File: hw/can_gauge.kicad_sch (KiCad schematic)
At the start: 22 parts, among them U1 MCP2515-xSO, U2 ULN2003A, U3 ULN2003A, U4 ULN2003A, U5 74HC595, U6 74HC595, U7 74HC595

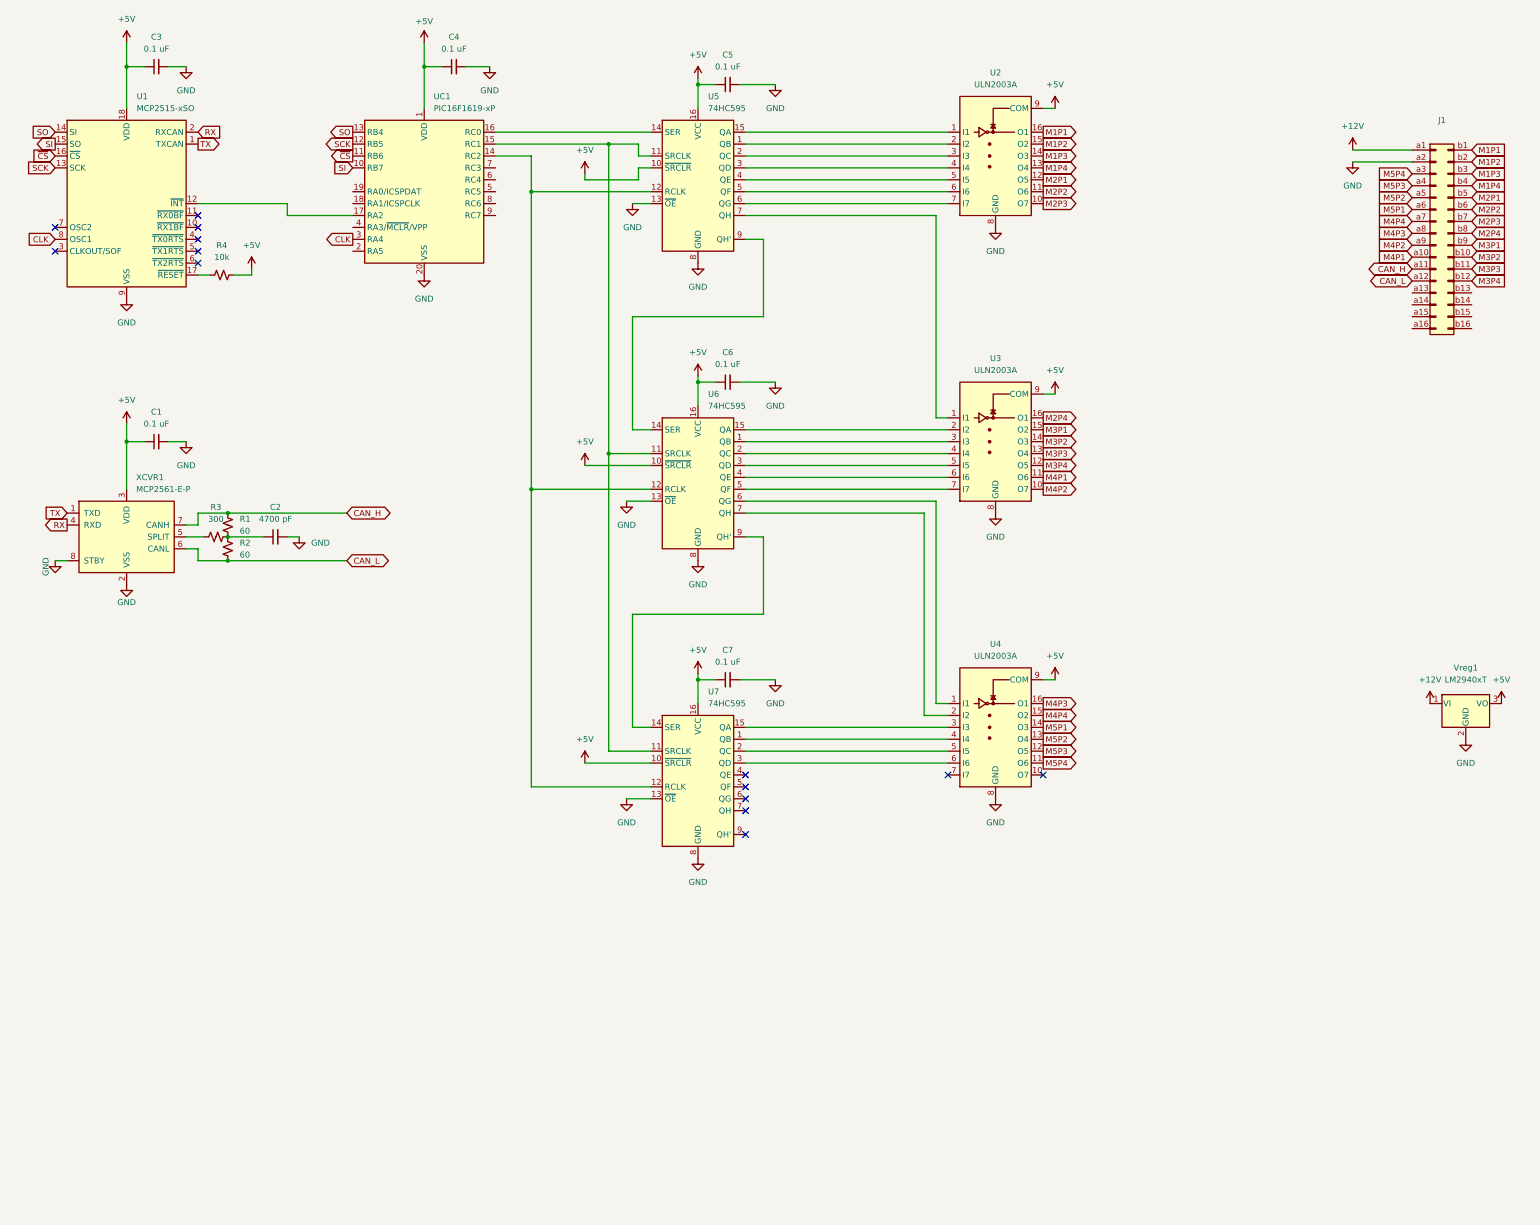
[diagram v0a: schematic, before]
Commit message: hw: switch to pic16f1459
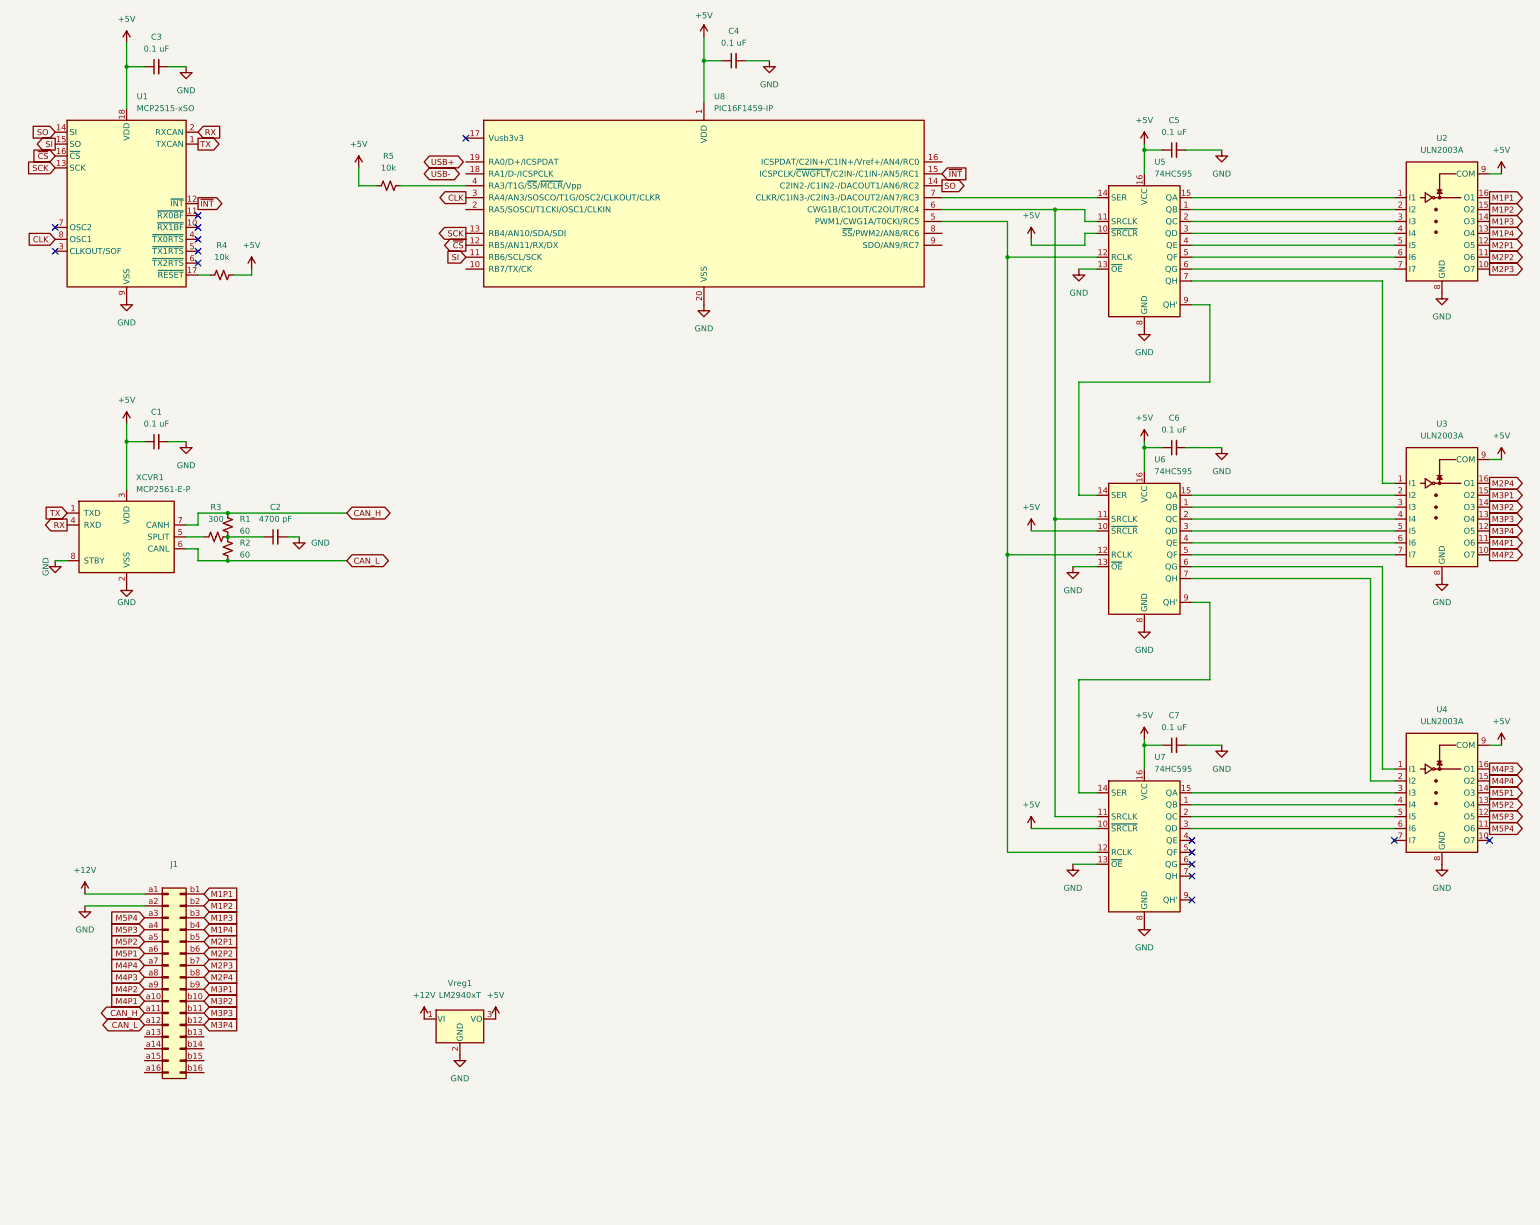
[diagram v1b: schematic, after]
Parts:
- removed UC1: PIC16F1619-xP, Package_DIP:DIP-20_W7.62mm, symbol MCU_Microchip_PIC16:PIC16F1619-xP
- added R5: 10k, symbol Device:R_Small_US
- added U8: PIC16F1459-IP, symbol MCU_Microchip_PIC16:PIC16F1459-IP
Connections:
- net +5V: now also R5.1, U8.1 (VDD)
- net CLK: now also U8.3 (RA4/AN3/SOSCO/T1G/OSC2/CLKOUT/CLKR)
- net GND: now also U8.20 (VSS)
- net SCK: now also U8.13 (RB4/AN10/SDA/SDI)
- net SI: now also U8.11 (RB6/SCL/SCK)
- net SO: now also U8.14 (C2IN2-/C1IN2-/DACOUT1/AN6/RC2)
- net ~{CS}: now also U8.12 (RB5/AN11/RX/DX)
- net at U5.11 (SRCLK), U6.11 (SRCLK), U7.11 (SRCLK): now also U8.6 (CWG1B/C1OUT/C2OUT/RC4)
- net at U5.12 (RCLK), U6.12 (RCLK), U7.12 (RCLK): now also U8.5 (PWM1/CWG1A/T0CKI/RC5)
- net at U5.14 (SER): now also U8.7 (CLKR/C1IN3-/C2IN3-/DACOUT2/AN7/RC3)
- net ~{INT}: now reaches U1.12 (~{INT})
- net ~{INT}: now also U8.15 (ICSPCLK/~{CWGFLT}/C2IN-/C1IN-/AN5/RC1)
- new net: R5.2, U8.4 (RA3/T1G/~{SS}/~{MCLR}/Vpp)
- no-connect marks 14 -> 15
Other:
- moved on the sheet: C4, C5, C6, C7, J1, U2, U3, U4, U5, U6, U7, Vreg1

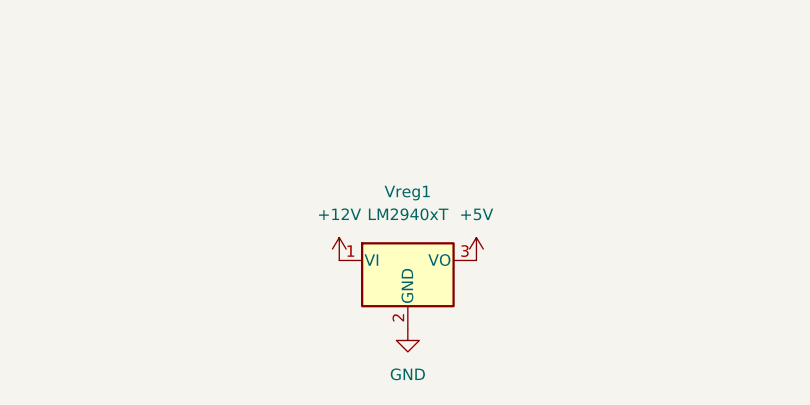
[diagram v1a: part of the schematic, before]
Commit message: hw: ldo caps
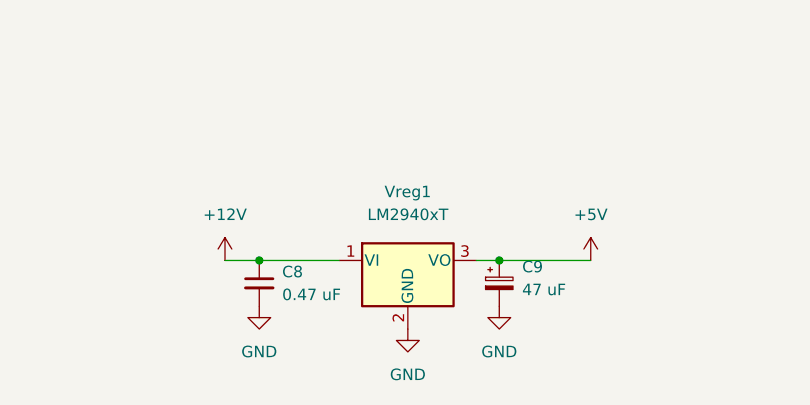
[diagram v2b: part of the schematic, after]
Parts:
- added C8: 0.47 uF, Capacitor_THT:C_Disc_D5.0mm_W2.5mm_P2.50mm, symbol Device:C_Small
- added C9: 47 uF, symbol Device:C_Polarized_Small
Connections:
- net +12V: now also C8.1
- net +5V: now also C9.1
- net GND: now also C8.2, C9.2

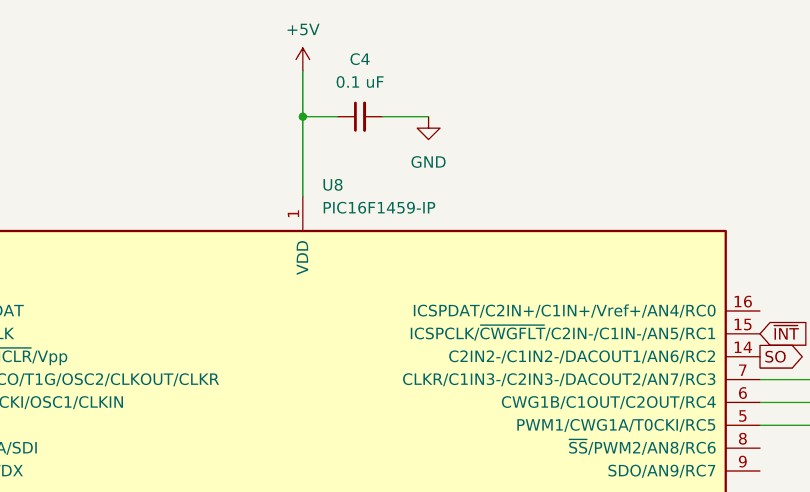
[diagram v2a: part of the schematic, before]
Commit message: hw: rename ICs
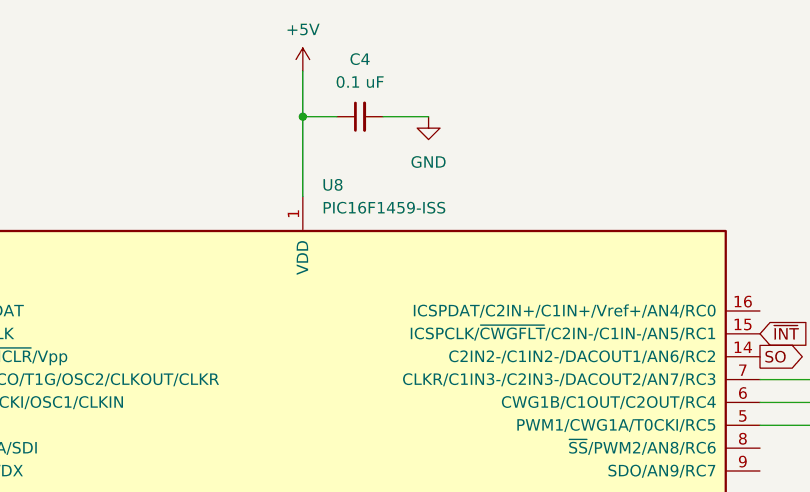
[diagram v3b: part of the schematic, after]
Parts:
- removed U8: PIC16F1459-IP, symbol MCU_Microchip_PIC16:PIC16F1459-IP
- added U8: PIC16F1459-ISS, symbol MCU_Microchip_PIC16:PIC16F1459-ISS
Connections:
- net +5V: now also U8.1 (VDD)
- net CLK: now also U8.3 (RA4/AN3/SOSCO/T1G/OSC2/CLKOUT/CLKR)
- net GND: now also U8.20 (VSS)
- net SCK: now also U8.13 (RB4/AN10/SDA/SDI)
- net SI: now also U8.11 (RB6/SCL/SCK)
- net SO: now also U8.14 (C2IN2-/C1IN2-/DACOUT1/AN6/RC2)
- net ~{CS}: now also U8.12 (RB5/AN11/RX/DX)
- net ~{INT}: now also U8.15 (ICSPCLK/~{CWGFLT}/C2IN-/C1IN-/AN5/RC1)
- net at R5.2: now also U8.4 (RA3/T1G/~{SS}/~{MCLR}/Vpp)
- net at U5.12 (RCLK), U6.12 (RCLK), U7.12 (RCLK): now also U8.5 (PWM1/CWG1A/T0CKI/RC5)
- net at U5.11 (SRCLK), U6.11 (SRCLK), U7.11 (SRCLK): now also U8.6 (CWG1B/C1OUT/C2OUT/RC4)
- net at U5.14 (SER): now also U8.7 (CLKR/C1IN3-/C2IN3-/DACOUT2/AN7/RC3)
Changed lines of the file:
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@@
 	)
 	(symbol
-		(lib_id "MCU_Microchip_PIC16:PIC16F1459-IP")
+		(lib_id "MCU_Microchip_PIC16:PIC16F1459-ISS")
 		(at 173.99 52.07 0)
 		(unit 1)
@@
 			)
 		)
-		(property "Value" "PIC16F1459-IP"
+		(property "Value" "PIC16F1459-ISS"
 			(at 176.1333 35.56 0)
 			(effects
@@
 			)
 		)
-		(pin "8"
+		(pin "7"
 		)
-		(pin "12"
-		)
-		(pin "20"
-		)
-		(pin "13"
-		)
-		(pin "19"
+		(pin "9"
 		)
 		(pin "5"
 		)
-		(pin "1"
+		(pin "17"
 		)
-		(pin "10"
+		(pin "16"
 		)
 		(pin "6"
 		)
-		(pin "9"
-		)
-		(pin "11"
-		)
-		(pin "15"
-		)
-		(pin "7"
-		)
-		(pin "16"
-		)
-		(pin "14"
-		)
-		(pin "18"
-		)
-		(pin "4"
-		)
-		(pin "17"
+		(pin "1"
 		)
 		(pin "3"
@@
 		(pin "2"
 		)
+		(pin "8"
+		)
+		(pin "13"
+		)
+		(pin "20"
+		)
+		(pin "12"
+		)
+		(pin "11"
+		)
+		(pin "10"
+		)
+		(pin "18"
+		)
+		(pin "19"
+		)
+		(pin "4"
+		)
+		(pin "15"
+		)
+		(pin "14"
+		)
 		(instances

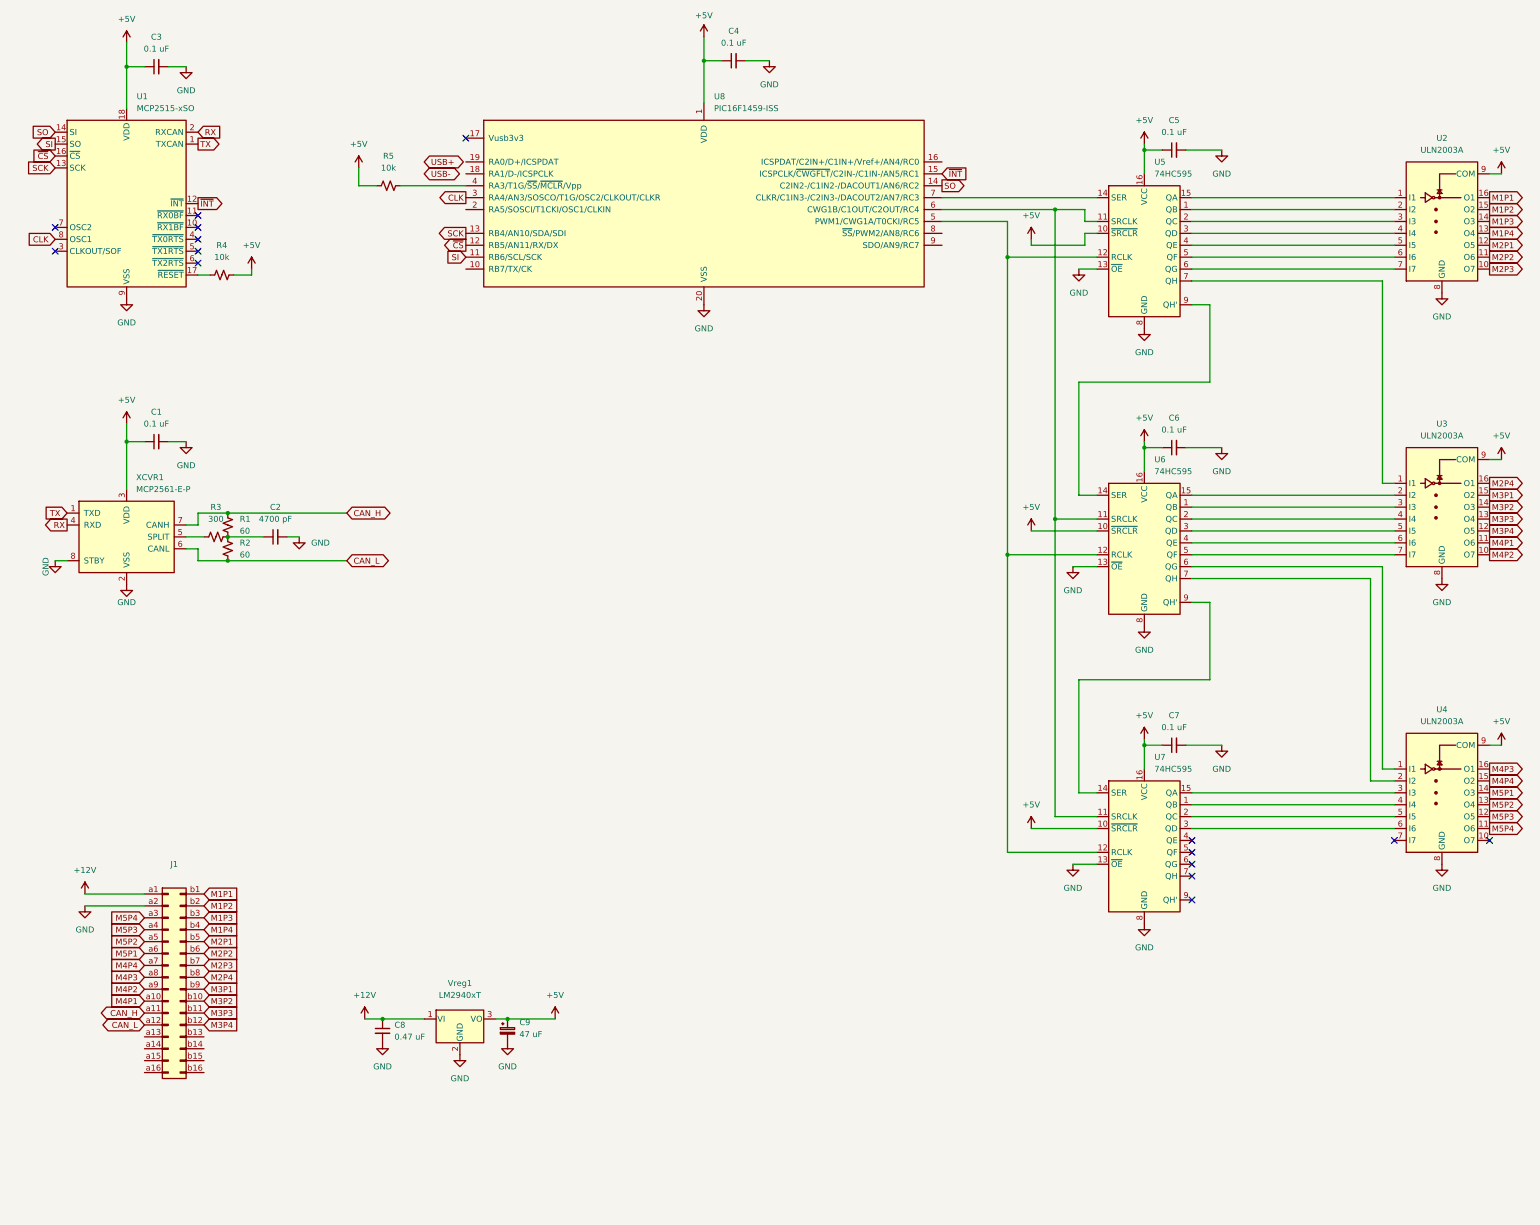
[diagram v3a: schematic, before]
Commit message: hw: not terminating node
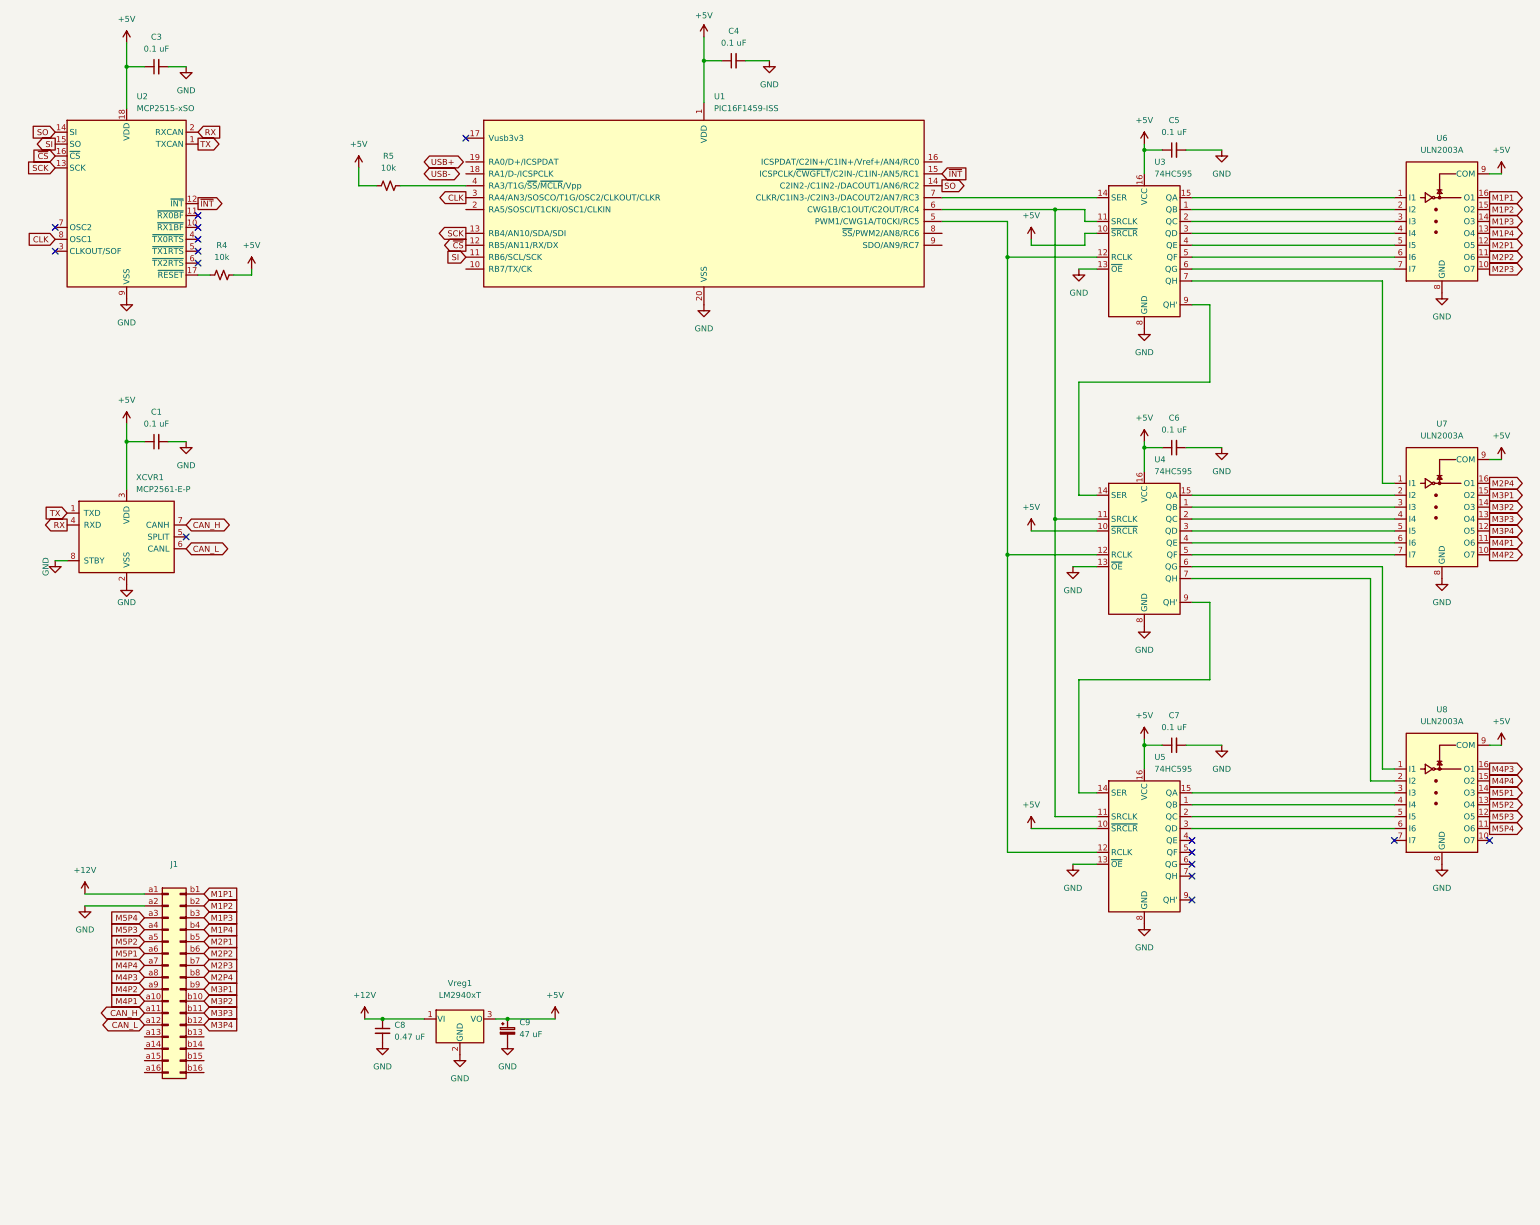
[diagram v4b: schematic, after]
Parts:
- removed C2: 4700 pF, symbol Device:C_Small
- removed R1, R2: 60, symbol Device:R_Small_US
- removed R3: 300, symbol Device:R_Small_US
- renumbered U8 to U1, U1 to U2, U5 to U3, U6 to U4, U7 to U5, U2 to U6, U3 to U7, U4 to U8
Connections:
- no-connect marks 15 -> 16
